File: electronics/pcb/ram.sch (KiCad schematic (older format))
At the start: 22 parts, among them U1 AS4C512M16D3L-12BIN

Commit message: Schematic review.
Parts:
- added C32: 100nF, Capacitor_SMD:C_0402_1005Metric, symbol Device:C_Small
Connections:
- net GND: now also C32.2
- net at C1.2, C2.1, C3.1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: now also C32.1
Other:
- moved on the sheet: C3
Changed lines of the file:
@@
 $Descr A4 11693 8268
 encoding utf-8
-Sheet 3 4
+Sheet 2 4
 Title ""
 Date ""
@@
 U 1 1 605A0A49
 P 7450 4450
-F 0 "C2" H 7542 4496 50  0000 L CNN
-F 1 "100nF" H 7542 4405 50  0000 L CNN
+F 0 "C2" H 7500 4550 50  0000 L CNN
+F 1 "100nF" H 7500 4350 50  0000 L CNN
 F 2 "Capacitor_SMD:C_0402_1005Metric" H 7450 4450 50  0001 C CNN
 F 3 "~" H 7450 4450 50  0001 C CNN
@@
 	8150 4250 8250 4250
 Wire Wire Line
-	7450 4250 8150 4250
+	7450 4250 7750 4250
 Connection ~ 8150 4250
 $Comp
 L Device:C_Small C3
 U 1 1 605F363F
-P 8150 4500
-F 0 "C3" H 8242 4546 50  0000 L CNN
-F 1 "100nF" H 8242 4455 50  0000 L CNN
-F 2 "Capacitor_SMD:C_0402_1005Metric" H 8150 4500 50  0001 C CNN
-F 3 "~" H 8150 4500 50  0001 C CNN
-	1    8150 4500
-	1    0    0    -1
-$EndComp
-Wire Wire Line
-	8150 4250 8150 4400
-Wire Wire Line
-	8150 4600 8150 4750
-$Comp
-L power:GND #PWR0105
-U 1 1 60626A0F
-P 8150 4750
-F 0 "#PWR0105" H 8150 4500 50  0001 C CNN
-F 1 "GND" H 8155 4577 50  0000 C CNN
-F 2 "" H 8150 4750 50  0001 C CNN
-F 3 "" H 8150 4750 50  0001 C CNN
-	1    8150 4750
+P 8050 4450
+F 0 "C3" H 8100 4550 50  0000 L CNN
+F 1 "100nF" H 8100 4350 50  0000 L CNN
+F 2 "Capacitor_SMD:C_0402_1005Metric" H 8050 4450 50  0001 C CNN
+F 3 "~" H 8050 4450 50  0001 C CNN
+	1    8050 4450
 	1    0    0    -1
 $EndComp
@@
 Wire Wire Line
 	5700 3450 5700 3200
+$Comp
+L Device:C_Small C32
+U 1 1 60A2394D
+P 7750 4450
+F 0 "C32" H 7800 4550 50  0000 L CNN
+F 1 "100nF" H 7800 4350 50  0000 L CNN
+F 2 "Capacitor_SMD:C_0402_1005Metric" H 7750 4450 50  0001 C CNN
+F 3 "~" H 7750 4450 50  0001 C CNN
+	1    7750 4450
+	1    0    0    -1
+$EndComp
+Wire Wire Line
+	7750 4250 7750 4350
+Connection ~ 7750 4250
+Wire Wire Line
+	7750 4250 8050 4250
+Wire Wire Line
+	7750 4550 7750 4600
+Wire Wire Line
+	7750 4600 7450 4600
+Connection ~ 7450 4600
+Wire Wire Line
+	8050 4550 8050 4600
+Wire Wire Line
+	8050 4600 7750 4600
+Connection ~ 7750 4600
+Wire Wire Line
+	8050 4350 8050 4250
+Connection ~ 8050 4250
+Wire Wire Line
+	8050 4250 8150 4250
 Wire Bus Line
 	1450 3050 1450 3350

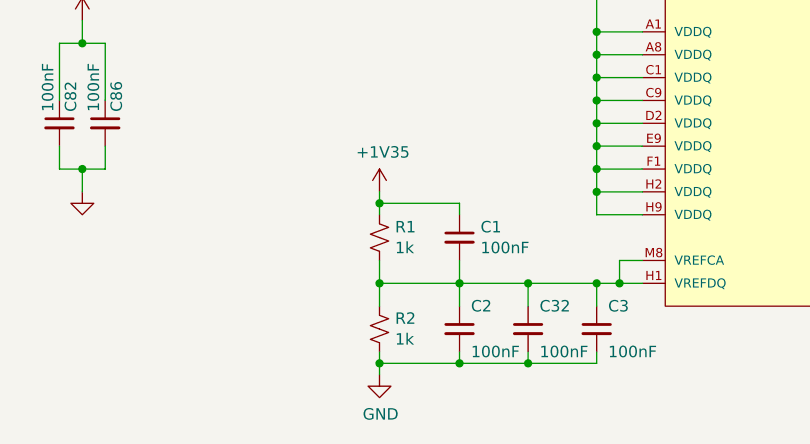
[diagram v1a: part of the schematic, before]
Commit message: Added tolerances
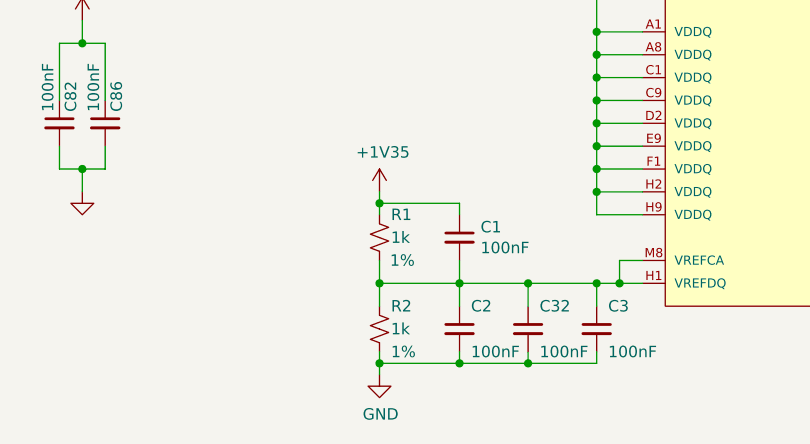
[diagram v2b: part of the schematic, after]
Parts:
- R1, R2: Tolerance (none) -> 1%
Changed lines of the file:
@@
 U 1 1 605988F8
 P 7100 4050
-F 0 "R1" H 7168 4096 50  0000 L CNN
-F 1 "1k" H 7168 4005 50  0000 L CNN
+F 0 "R1" H 7150 4150 50  0000 L CNN
+F 1 "1k" H 7150 4050 50  0000 L CNN
 F 2 "Resistor_SMD:R_0402_1005Metric" H 7100 4050 50  0001 C CNN
 F 3 "~" H 7100 4050 50  0001 C CNN
+F 4 "1%" H 7200 3950 50  0000 C CNN "Tolerance"
 	1    7100 4050
 	1    0    0    -1
@@
 U 1 1 6059FB05
 P 7100 4450
-F 0 "R2" H 7168 4496 50  0000 L CNN
-F 1 "1k" H 7168 4405 50  0000 L CNN
+F 0 "R2" H 7150 4550 50  0000 L CNN
+F 1 "1k" H 7150 4450 50  0000 L CNN
 F 2 "Resistor_SMD:R_0402_1005Metric" H 7100 4450 50  0001 C CNN
 F 3 "~" H 7100 4450 50  0001 C CNN
+F 4 "1%" H 7150 4350 50  0000 L CNN "Tolerance"
 	1    7100 4450
 	1    0    0    -1

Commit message: DRC + BOM script
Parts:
- U1: MPN (none) -> AS4C512M16D3L-12BIN; automotive No -> (none); category IC -> (none); device class L1 Integrated Circuits (ICs) -> (none); device class L2 Memory -> (none); device class L3 RAM -> (none); digikey description IC DRAM 8G PARALLEL 96FBGA -> (none); digikey part number 1450-1272-ND -> (none); frequency 800MHz -> (none); height 1.2mm -> (none); interface Parallel -> (none); ipc land pattern name BGA144N80P9X16_1400X900X110 -> (none); lead free Yes -> (none); library id d1b2570ed0e6ca77 -> (none); manufacturer Alliance Memory -> (none); max supply voltage 1.45V -> (none); memory size 8Gbits -> (none); memory type SDRAM -> (none); min supply voltage 1.283V -> (none); mouser description AS4C512xx Series 8 Gb (512 M x 16) 800 MHz Surface Mount DD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 -> (none); mouser part number 913-512M16D3L12BIN -> (none); package FBGA96 -> (none); rohs Yes -> (none); standoff height 0.135mm -> (none); temperature range high +95°C -> (none); temperature range low -40°C -> (none)
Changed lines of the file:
@@
 F 2 "AS4C512M16D3L:Alliance_Memory-AS4C512M16D3L-12BIN-0-0-IPC_A" H 1750 1650 50  0001 L CNN
 F 3 "https://www.alliancememory.com/wp-content/uploads/pdf/ddr3/20160614%20-%208GB_DDR3L_AS4C512M16D3L_AS4C1G8MD3L%20revised%20v%202.0%20June%202016.pdf" H 1750 1750 50  0001 L CNN
-F 4 "No" H 1750 1850 50  0001 L CNN "automotive"
-F 5 "IC" H 1750 1950 50  0001 L CNN "category"
-F 6 "Integrated Circuits (ICs)" H 1750 2050 50  0001 L CNN "device class L1"
-F 7 "Memory" H 1750 2150 50  0001 L CNN "device class L2"
-F 8 "RAM" H 1750 2250 50  0001 L CNN "device class L3"
-F 9 "IC DRAM 8G PARALLEL 96FBGA" H 1750 2350 50  0001 L CNN "digikey description"
-F 10 "1450-1272-ND" H 1750 2450 50  0001 L CNN "digikey part number"
-F 11 "800MHz" H 1750 2550 50  0001 L CNN "frequency"
-F 12 "1.2mm" H 1750 2650 50  0001 L CNN "height"
-F 13 "Parallel" H 1750 2750 50  0001 L CNN "interface"
-F 14 "BGA144N80P9X16_1400X900X110" H 1750 2850 50  0001 L CNN "ipc land pattern name"
-F 15 "Yes" H 1750 2950 50  0001 L CNN "lead free"
-F 16 "d1b2570ed0e6ca77" H 1750 3050 50  0001 L CNN "library id"
-F 17 "Alliance Memory" H 1750 3150 50  0001 L CNN "manufacturer"
-F 18 "1.45V" H 1750 3250 50  0001 L CNN "max supply voltage"
-F 19 "8Gbits" H 1750 3350 50  0001 L CNN "memory size"
-F 20 "SDRAM" H 1750 3450 50  0001 L CNN "memory type"
-F 21 "1.283V" H 1750 3550 50  0001 L CNN "min supply voltage"
-F 22 "AS4C512xx Series 8 Gb (512 M x 16) 800 MHz Surface Mount DDR3L SDRAM - FBGA-96" H 1750 3650 50  0001 L CNN "mouser description"
-F 23 "913-512M16D3L12BIN" H 1750 3750 50  0001 L CNN "mouser part number"
-F 24 "FBGA96" H 1750 3850 50  0001 L CNN "package"
-F 25 "Yes" H 1750 3950 50  0001 L CNN "rohs"
-F 26 "0.135mm" H 1750 4050 50  0001 L CNN "standoff height"
-F 27 "+95°C" H 1750 4150 50  0001 L CNN "temperature range high"
-F 28 "-40°C" H 1750 4250 50  0001 L CNN "temperature range low"
+F 4 "AS4C512M16D3L-12BIN" H 1750 1250 50  0001 C CNN "MPN"
 	2    1750 1250
 	1    0    0    -1

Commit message: Removed all the extra fields
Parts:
- U1: automotive No -> (none); category IC -> (none); device class L1 Integrated Circuits (ICs) -> (none); device class L2 Memory -> (none); device class L3 RAM -> (none); digikey description IC DRAM 8G PARALLEL 96FBGA -> (none); digikey part number 1450-1272-ND -> (none); frequency 800MHz -> (none); height 1.2mm -> (none); interface Parallel -> (none); ipc land pattern name BGA144N80P9X16_1400X900X110 -> (none); lead free Yes -> (none); library id d1b2570ed0e6ca77 -> (none); manufacturer Alliance Memory -> (none); max supply voltage 1.45V -> (none); memory size 8Gbits -> (none); memory type SDRAM -> (none); min supply voltage 1.283V -> (none); mouser description AS4C512xx Series 8 Gb (512 M x 16) 800 MHz Surface Mount DD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 -> (none); mouser part number 913-512M16D3L12BIN -> (none); package FBGA96 -> (none); rohs Yes -> (none); standoff height 0.135mm -> (none); temperature range high +95°C -> (none); temperature range low -40°C -> (none)
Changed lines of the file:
@@
 F 2 "AS4C512M16D3L:Alliance_Memory-AS4C512M16D3L-12BIN-0-0-IPC_A" H 8150 2550 50  0001 L CNN
 F 3 "https://www.alliancememory.com/wp-content/uploads/pdf/ddr3/20160614%20-%208GB_DDR3L_AS4C512M16D3L_AS4C1G8MD3L%20revised%20v%202.0%20June%202016.pdf" H 8150 2650 50  0001 L CNN
-F 4 "No" H 8150 2750 50  0001 L CNN "automotive"
-F 5 "IC" H 8150 2850 50  0001 L CNN "category"
-F 6 "Integrated Circuits (ICs)" H 8150 2950 50  0001 L CNN "device class L1"
-F 7 "Memory" H 8150 3050 50  0001 L CNN "device class L2"
-F 8 "RAM" H 8150 3150 50  0001 L CNN "device class L3"
-F 9 "IC DRAM 8G PARALLEL 96FBGA" H 8150 3250 50  0001 L CNN "digikey description"
-F 10 "1450-1272-ND" H 8150 3350 50  0001 L CNN "digikey part number"
-F 11 "800MHz" H 8150 3450 50  0001 L CNN "frequency"
-F 12 "1.2mm" H 8150 3550 50  0001 L CNN "height"
-F 13 "Parallel" H 8150 3650 50  0001 L CNN "interface"
-F 14 "BGA144N80P9X16_1400X900X110" H 8150 3750 50  0001 L CNN "ipc land pattern name"
-F 15 "Yes" H 8150 3850 50  0001 L CNN "lead free"
-F 16 "d1b2570ed0e6ca77" H 8150 3950 50  0001 L CNN "library id"
-F 17 "Alliance Memory" H 8150 4050 50  0001 L CNN "manufacturer"
-F 18 "1.45V" H 8150 4150 50  0001 L CNN "max supply voltage"
-F 19 "8Gbits" H 8150 4250 50  0001 L CNN "memory size"
-F 20 "SDRAM" H 8150 4350 50  0001 L CNN "memory type"
-F 21 "1.283V" H 8150 4450 50  0001 L CNN "min supply voltage"
-F 22 "AS4C512xx Series 8 Gb (512 M x 16) 800 MHz Surface Mount DDR3L SDRAM - FBGA-96" H 8150 4550 50  0001 L CNN "mouser description"
-F 23 "913-512M16D3L12BIN" H 8150 4650 50  0001 L CNN "mouser part number"
-F 24 "FBGA96" H 8150 4750 50  0001 L CNN "package"
-F 25 "Yes" H 8150 4850 50  0001 L CNN "rohs"
-F 26 "0.135mm" H 8150 4950 50  0001 L CNN "standoff height"
-F 27 "+95°C" H 8150 5050 50  0001 L CNN "temperature range high"
-F 28 "-40°C" H 8150 5150 50  0001 L CNN "temperature range low"
 	1    8150 2150
 	1    0    0    -1

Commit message: Added in all the part numbers
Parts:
- C1, C2, C3, C32, C74, C75, C76, C77, C78, C79, C80, C82, C85, C86, C87, C89, C90, C91, C92: MPN (none) -> CC0402KRX7R7BB104
- R1, R2: MPN (none) -> 4-1879208-9
- R3: MPN (none) -> 0402WGF2400TCE; Tolerance (none) -> 1%
- U1: MPN (none) -> AS4C512M16D3L-12BIN

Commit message: Part numbers are _properly_ in now.
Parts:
- R3: Tolerance 1% -> (none)
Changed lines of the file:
@@
 F 3 "~" H 1750 1750 50 0001 L CNN
 F 4 "AS4C512M16D3L-12BIN" H 1750 1250 50 0001 C CNN "MPN"
+F 5 "~" H 2400 1615 50 0001 C CNN "Tolerance"
 	2    1750 1250
 	1    0    0    -1
@@
 F 3 "~" H 7450 4050 50 0001 C CNN
 F 4 "CC0402KRX7R7BB104" H 7542 4196 50 0001 C CNN "MPN"
+F 5 "~" H 7542 4196 50 0001 C CNN "Tolerance"
 	1    7450 4050
 	1    0    0    -1
@@
 F 3 "~" H 7450 4450 50 0001 C CNN
 F 4 "CC0402KRX7R7BB104" H 7500 4650 50 0001 C CNN "MPN"
+F 5 "~" H 7500 4650 50 0001 C CNN "Tolerance"
 	1    7450 4450
 	1    0    0    -1
@@
 F 3 "~" H 8050 4450 50 0001 C CNN
 F 4 "CC0402KRX7R7BB104" H 8100 4650 50 0001 C CNN "MPN"
+F 5 "~" H 8100 4650 50 0001 C CNN "Tolerance"
 	1    8050 4450
 	1    0    0    -1
@@
 F 3 "~" H 3150 4050 50 0001 C CNN
 F 4 "0402WGF2400TCE" H 3200 4250 50 0001 C CNN "MPN"
-F 5 "1%" H 3200 4250 50 0001 C CNN "Tolerance"
+F 5 "~" H 3200 4250 50 0001 C CNN "Tolerance"
 	1    3150 4050
 	0    1    1    0
@@
 F 3 "~" H 4600 2300 50 0001 C CNN
 F 4 "CC0402KRX7R7BB104" H 4650 2450 50 0001 C CNN "MPN"
+F 5 "~" H 4650 2450 50 0001 C CNN "Tolerance"
 	1    4600 2300
 	1    0    0    -1
@@
 F 3 "~" H 4800 2300 50 0001 C CNN
 F 4 "CC0402KRX7R7BB104" H 4850 2450 50 0001 C CNN "MPN"
+F 5 "~" H 4850 2450 50 0001 C CNN "Tolerance"
 	1    4800 2300
 	1    0    0    -1
@@
 F 3 "~" H 5000 2300 50 0001 C CNN
 F 4 "CC0402KRX7R7BB104" H 5050 2450 50 0001 C CNN "MPN"
+F 5 "~" H 5050 2450 50 0001 C CNN "Tolerance"
 	1    5000 2300
 	1    0    0    -1
@@
 F 3 "~" H 5200 2300 50 0001 C CNN
 F 4 "CC0402KRX7R7BB104" H 5250 2450 50 0001 C CNN "MPN"
+F 5 "~" H 5250 2450 50 0001 C CNN "Tolerance"
 	1    5200 2300
 	1    0    0    -1
@@
 F 3 "~" H 5400 2300 50 0001 C CNN
 F 4 "CC0402KRX7R7BB104" H 5450 2450 50 0001 C CNN "MPN"
+F 5 "~" H 5450 2450 50 0001 C CNN "Tolerance"
 	1    5400 2300
 	1    0    0    -1
@@
 F 3 "~" H 6000 2300 50 0001 C CNN
 F 4 "CC0402KRX7R7BB104" H 6050 2450 50 0001 C CNN "MPN"
+F 5 "~" H 6050 2450 50 0001 C CNN "Tolerance"
 	1    6000 2300
 	1    0    0    -1
@@
 F 3 "~" H 6200 2300 50 0001 C CNN
 F 4 "CC0402KRX7R7BB104" H 6250 2450 50 0001 C CNN "MPN"
+F 5 "~" H 6250 2450 50 0001 C CNN "Tolerance"
 	1    6200 2300
 	1    0    0    -1
@@
 F 3 "~" H 6400 2300 50 0001 C CNN
 F 4 "CC0402KRX7R7BB104" H 6450 2450 50 0001 C CNN "MPN"
+F 5 "~" H 6450 2450 50 0001 C CNN "Tolerance"
 	1    6400 2300
 	1    0    0    -1
@@
 F 3 "~" H 6600 2300 50 0001 C CNN
 F 4 "CC0402KRX7R7BB104" H 6650 2450 50 0001 C CNN "MPN"
+F 5 "~" H 6650 2450 50 0001 C CNN "Tolerance"
 	1    6600 2300
 	1    0    0    -1
@@
 F 3 "~" H 6800 2300 50 0001 C CNN
 F 4 "CC0402KRX7R7BB104" H 6850 2450 50 0001 C CNN "MPN"
+F 5 "~" H 6850 2450 50 0001 C CNN "Tolerance"
 	1    6800 2300
 	1    0    0    -1
@@
 F 3 "~" H 7000 2300 50 0001 C CNN
 F 4 "CC0402KRX7R7BB104" H 7050 2450 50 0001 C CNN "MPN"
+F 5 "~" H 7050 2450 50 0001 C CNN "Tolerance"
 	1    7000 2300
 	1    0    0    -1
@@
 F 3 "~" H 8150 2650 50 0001 L CNN
 F 4 "AS4C512M16D3L-12BIN" H 8900 2515 50 0001 C CNN "MPN"
+F 5 "~" H 8900 2515 50 0001 C CNN "Tolerance"
 	1    8150 2150
 	1    0    0    -1
@@
 F 3 "~" H 5600 2300 50 0001 C CNN
 F 4 "CC0402KRX7R7BB104" H 5650 2450 50 0001 C CNN "MPN"
+F 5 "~" H 5650 2450 50 0001 C CNN "Tolerance"
 	1    5600 2300
 	1    0    0    -1
@@
 F 3 "~" H 5800 2300 50 0001 C CNN
 F 4 "CC0402KRX7R7BB104" H 5850 2450 50 0001 C CNN "MPN"
+F 5 "~" H 5850 2450 50 0001 C CNN "Tolerance"
 	1    5800 2300
 	1    0    0    -1
@@
 F 3 "~" H 5700 3550 50 0001 C CNN
 F 4 "CC0402KRX7R7BB104" H 5750 3700 50 0001 C CNN "MPN"
+F 5 "~" H 5750 3700 50 0001 C CNN "Tolerance"
 	1    5700 3550
 	1    0    0    -1
@@
 F 3 "~" H 5900 3550 50 0001 C CNN
 F 4 "CC0402KRX7R7BB104" H 5950 3700 50 0001 C CNN "MPN"
+F 5 "~" H 5950 3700 50 0001 C CNN "Tolerance"
 	1    5900 3550
 	1    0    0    -1
@@
 F 3 "~" H 7750 4450 50 0001 C CNN
 F 4 "CC0402KRX7R7BB104" H 7800 4650 50 0001 C CNN "MPN"
+F 5 "~" H 7800 4650 50 0001 C CNN "Tolerance"
 	1    7750 4450
 	1    0    0    -1
